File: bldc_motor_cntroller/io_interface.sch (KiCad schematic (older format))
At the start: 28 parts, among them J1 SM06B-SRSS-TB(LF)(SN), J2 Conn_01x18, J3 SM04B-SRSS-TB(LF)(SN), J5 0473460001, J6 TC2030 Tag-connect, SW1 B3U-1000P-B, SW2 B3U-1000P-B, U1 TCAN332GDCNT

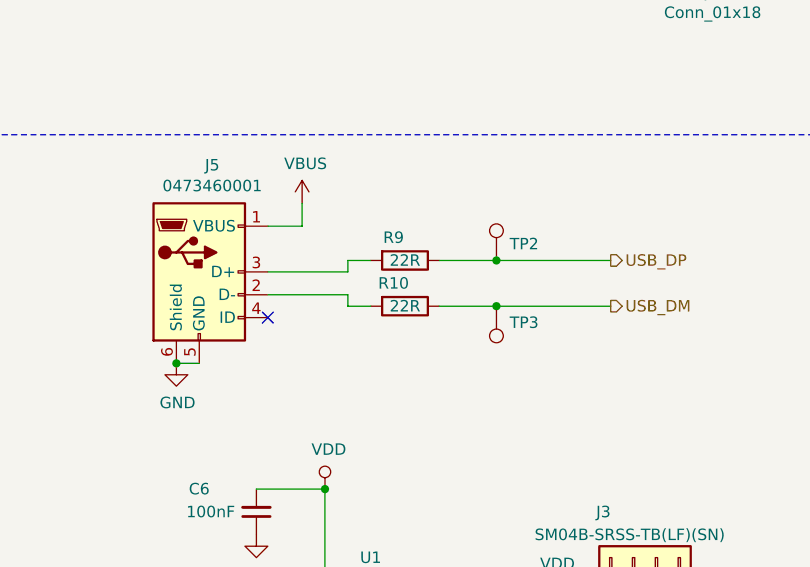
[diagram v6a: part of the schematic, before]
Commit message: improved BOM
Signed-off-by: azmat bilal <azmat.bilal@outlook.com>
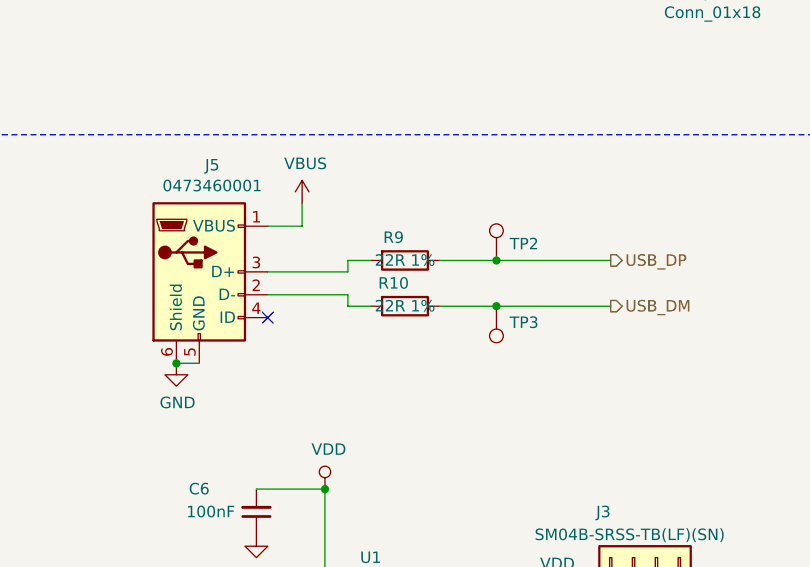
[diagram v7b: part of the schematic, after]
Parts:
- C1, C2, C3, C4, C5: MPN (none) -> VJ0402A820JXACW1BC
- C6: MPN (none) -> GRM155R62A104KE14D
- J1: MPN (none) -> SM06B-SRSS-TB(LF)(SN)
- J2, J6, TP2, TP3: MPN (none) -> -
- J3: MPN (none) -> SM04B-SRSS-TB(LF)(SN)
- J5: MPN (none) -> 0473460001
- R1, R2, R6, R7, R8: MPN (none) -> CRCW04020000Z0EDC
- R10, R9: value 22R -> 22R 1%; MPN (none) -> CRCW040222R0FKEDC
- R11: MPN (none) -> CRCW040210K0FKEDC
- R12: MPN (none) -> ERJ-2RKF1200X
- R3, R4, R5: MPN (none) -> CRCW04023K30FKEDC
- SW1, SW2: MPN (none) -> B3U-1000P-B
- U1: MPN (none) -> TCAN332GDCNT
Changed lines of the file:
@@
 F 2 "Resistor_SMD:R_0402_1005Metric" V 2380 1000 50  0001 C CNN
 F 3 "~" H 2450 1000 50  0001 C CNN
+F 4 "CRCW04020000Z0EDC" H 2450 1000 50  0001 C CNN "MPN"
 	1    2450 1000
 	0    1    1    0
@@
 F 2 "Capacitor_SMD:C_0402_1005Metric" H 2450 1150 50  0001 C CNN
 F 3 "~" H 2450 1150 50  0001 C CNN
+F 4 "VJ0402A820JXACW1BC" H 2450 1150 50  0001 C CNN "MPN"
 	1    2450 1150
 	0    1    1    0
@@
 F 2 "Resistor_SMD:R_0402_1005Metric" V 2380 1400 50  0001 C CNN
 F 3 "~" H 2450 1400 50  0001 C CNN
+F 4 "CRCW04020000Z0EDC" H 2450 1400 50  0001 C CNN "MPN"
 	1    2450 1400
 	0    1    1    0
@@
 F 2 "Capacitor_SMD:C_0402_1005Metric" H 2400 1550 50  0001 C CNN
 F 3 "~" H 2400 1550 50  0001 C CNN
+F 4 "VJ0402A820JXACW1BC" H 2400 1550 50  0001 C CNN "MPN"
 	1    2400 1550
 	0    1    1    0
@@
 F 2 "Resistor_SMD:R_0402_1005Metric" V 2380 2300 50  0001 C CNN
 F 3 "~" H 2450 2300 50  0001 C CNN
+F 4 "CRCW04020000Z0EDC" H 2450 2300 50  0001 C CNN "MPN"
 	1    2450 2300
 	0    1    1    0
@@
 F 2 "Capacitor_SMD:C_0402_1005Metric" H 2400 2450 50  0001 C CNN
 F 3 "~" H 2400 2450 50  0001 C CNN
+F 4 "VJ0402A820JXACW1BC" H 2400 2450 50  0001 C CNN "MPN"
 	1    2400 2450
 	0    1    1    0
@@
 F 2 "Resistor_SMD:R_0402_1005Metric" V 2380 2700 50  0001 C CNN
 F 3 "~" H 2450 2700 50  0001 C CNN
+F 4 "CRCW04020000Z0EDC" H 2450 2700 50  0001 C CNN "MPN"
 	1    2450 2700
 	0    1    1    0
@@
 F 2 "Capacitor_SMD:C_0402_1005Metric" H 2400 2850 50  0001 C CNN
 F 3 "~" H 2400 2850 50  0001 C CNN
+F 4 "VJ0402A820JXACW1BC" H 2400 2850 50  0001 C CNN "MPN"
 	1    2400 2850
 	0    1    1    0
@@
 F 2 "Resistor_SMD:R_0402_1005Metric" V 2380 3100 50  0001 C CNN
 F 3 "~" H 2450 3100 50  0001 C CNN
+F 4 "CRCW04020000Z0EDC" H 2450 3100 50  0001 C CNN "MPN"
 	1    2450 3100
 	0    1    1    0
@@
 F 2 "Capacitor_SMD:C_0402_1005Metric" H 2400 3250 50  0001 C CNN
 F 3 "~" H 2400 3250 50  0001 C CNN
+F 4 "VJ0402A820JXACW1BC" H 2400 3250 50  0001 C CNN "MPN"
 	1    2400 3250
 	0    1    1    0
@@
 F 2 "Connector:Tag-Connect_TC2030-IDC-NL_2x03_P1.27mm_Vertical" H 6950 5650 50  0001 C CNN
 F 3 "~" H 6950 5650 50  0001 C CNN
+F 4 "-" H 6950 5650 50  0001 C CNN "MPN"
 	1    6950 5650
 	1    0    0    -1
@@
 F 2 "Button_Switch_SMD:SW_SPST_B3U-1000P" H 6100 5850 50  0001 C CNN
 F 3 "~" H 6100 5850 50  0001 C CNN
+F 4 "B3U-1000P-B" H 6100 5650 50  0001 C CNN "MPN"
 	1    6100 5650
 	1    0    0    -1
@@
 F 2 "Button_Switch_SMD:SW_SPST_B3U-1000P" H 9500 5300 50  0001 C CNN
 F 3 "~" H 9500 5300 50  0001 C CNN
+F 4 "B3U-1000P-B" H 9500 5100 50  0001 C CNN "MPN"
 	1    9500 5100
 	0    1    1    0
@@
 F 2 "Resistor_SMD:R_0402_1005Metric" V 9430 5500 50  0001 C CNN
 F 3 "~" H 9500 5500 50  0001 C CNN
+F 4 "CRCW040210K0FKEDC" H 9500 5500 50  0001 C CNN "MPN"
 	1    9500 5500
 	-1   0    0    1
@@
 F 2 "Connector_USB:USB_Micro-B_Molex_47346-0001" H 2350 5050 50  0001 C CNN
 F 3 "~" H 2350 5050 50  0001 C CNN
+F 4 "0473460001" H 2200 5100 50  0001 C CNN "MPN"
 	1    2200 5100
 	1    0    0    -1
@@
 P 3100 5250
 F 0 "R10" V 3000 5200 50  0000 C CNN
-F 1 "22R" V 3100 5250 50  0000 C CNN
+F 1 "22R 1%" V 3100 5250 50  0000 C CNN
 F 2 "Resistor_SMD:R_0402_1005Metric" V 3030 5250 50  0001 C CNN
 F 3 "~" H 3100 5250 50  0001 C CNN
+F 4 "CRCW040222R0FKEDC" H 3100 5250 50  0001 C CNN "MPN"
 	1    3100 5250
 	0    1    1    0
@@
 P 3100 5050
 F 0 "R9" V 3000 5000 50  0000 C CNN
-F 1 "22R" V 3100 5050 50  0000 C CNN
+F 1 "22R 1%" V 3100 5050 50  0000 C CNN
 F 2 "Resistor_SMD:R_0402_1005Metric" V 3030 5050 50  0001 C CNN
 F 3 "~" H 3100 5050 50  0001 C CNN
+F 4 "CRCW040222R0FKEDC" H 3100 5050 50  0001 C CNN "MPN"
 	1    3100 5050
 	0    1    1    0
@@
 F 2 "TestPoint:TestPoint_Pad_D1.5mm" H 3700 5050 50  0001 C CNN
 F 3 "~" H 3700 5050 50  0001 C CNN
+F 4 "-" H 3500 5050 50  0001 C CNN "MPN"
 	1    3500 5050
 	1    0    0    -1
@@
 F 2 "TestPoint:TestPoint_Pad_D1.5mm" H 3700 5250 50  0001 C CNN
 F 3 "~" H 3700 5250 50  0001 C CNN
+F 4 "-" H 3500 5250 50  0001 C CNN "MPN"
 	1    3500 5250
 	-1   0    0    1
@@
 F 2 "Capacitor_SMD:C_0402_1005Metric" H 2450 6150 50  0001 C CNN
 F 3 "~" H 2450 6150 50  0001 C CNN
+F 4 "GRM155R62A104KE14D" H 2450 6150 50  0001 C CNN "MPN"
 	1    2450 6150
 	-1   0    0    1
@@
 F 2 "Package_TO_SOT_SMD:SOT-23-8" H 2750 6350 50  0001 C CIN
 F 3 "http://www.ti.com/lit/ds/symlink/tcan337.pdf" H 2750 6850 50  0001 C CNN
+F 4 "TCAN332GDCNT" H 2750 6850 50  0001 C CNN "MPN"
 	1    2750 6850
 	1    0    0    -1
@@
 F 2 "Connector_JST:JST_SH_SM06B-SRSS-TB_1x06-1MP_P1.00mm_Horizontal" H 8750 2000 50  0001 C CNN
 F 3 "~" H 8750 2000 50  0001 C CNN
+F 4 "SM06B-SRSS-TB(LF)(SN)" H 8750 2000 50  0001 C CNN "MPN"
 	1    8750 2000
 	1    0    0    -1
@@
 F 2 "Resistor_SMD:R_0402_1005Metric" V 6630 1750 50  0001 C CNN
 F 3 "~" H 6700 1750 50  0001 C CNN
+F 4 "CRCW04023K30FKEDC" H 6700 1750 50  0001 C CNN "MPN"
 	1    6700 1750
 	1    0    0    -1
@@
 F 2 "Resistor_SMD:R_0402_1005Metric" V 6430 1750 50  0001 C CNN
 F 3 "~" H 6500 1750 50  0001 C CNN
+F 4 "CRCW04023K30FKEDC" H 6500 1750 50  0001 C CNN "MPN"
 	1    6500 1750
 	1    0    0    -1
@@
 F 2 "Resistor_SMD:R_0402_1005Metric" V 6230 1750 50  0001 C CNN
 F 3 "~" H 6300 1750 50  0001 C CNN
+F 4 "CRCW04023K30FKEDC" H 6300 1750 50  0001 C CNN "MPN"
 	1    6300 1750
 	1    0    0    -1
@@
 F 2 "Connector_PinHeader_2.54mm:PinHeader_1x18_P2.54mm_Horizontal" H 4500 3750 50  0001 C CNN
 F 3 "~" H 4500 3750 50  0001 C CNN
+F 4 "-" H 4500 3750 50  0001 C CNN "MPN"
 	1    4500 3750
 	0    1    1    0
@@
 F 2 "Connector_JST:JST_SH_SM04B-SRSS-TB_1x04-1MP_P1.00mm_Horizontal" H 4100 6350 50  0001 C CNN
 F 3 "~" H 4100 6350 50  0001 C CNN
+F 4 "SM04B-SRSS-TB(LF)(SN)" H 4100 6350 50  0001 C CNN "MPN"
 	1    4100 6350
 	0    -1   -1   0
@@
 F 2 "Resistor_SMD:R_0402_1005Metric" V 3480 6850 50  0001 C CNN
 F 3 "~" H 3550 6850 50  0001 C CNN
+F 4 "ERJ-2RKF1200X" H 3550 6850 50  0001 C CNN "MPN"
 	1    3550 6850
 	-1   0    0    1
